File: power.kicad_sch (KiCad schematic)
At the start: 14 parts, among them J3 Conn_01x02, U1 TP4056-42-ESOP8, U11 TPS62170DSG

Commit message: finish power management
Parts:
- added D4: D, symbol Device:D
- added J4: USB_C_Receptacle_PowerOnly_6P, symbol Connector:USB_C_Receptacle_PowerOnly_6P
- added Q1: AO3401A, Package_TO_SOT_SMD:SOT-23, symbol Transistor_FET:AO3401A
- added R10: 100k, Resistor_SMD:R_0603_1608Metric, symbol Device:R
- added R6: 562k, Resistor_SMD:R_0603_1608Metric, symbol Device:R
- added R7: 180k, Resistor_SMD:R_0603_1608Metric, symbol Device:R
- added R8, R9: 5.1k, Resistor_SMD:R_0603_1608Metric, symbol Device:R
- C3, C4, C6, C7: footprint (none) -> Capacitor_SMD:C_0603_1608Metric
- D1: value LED -> GREEN; footprint (none) -> LED_SMD:LED_0603_1608Metric; LCSC (none) -> C965804; Manufacturer (none) -> XINGLIGHT; Manufacturer Part Number (none) -> XL-1608UGC-04
- D2: value LED -> RED; footprint (none) -> LED_SMD:LED_0603_1608Metric; LCSC (none) -> C965799; Manufacturer (none) -> XINGLIGHT; Manufacturer Part Number (none) -> XL-1608SURC-06
- J3: LCSC (none) -> C131337; Manufacturer (none) -> JST; Manufacturer Part Number (none) -> B2B-PH-K-S(LF)(SN)
- L1: value 22uH -> 2.2uH; LCSC C128694 -> C5349701; Manufacturer SXN -> APV; Manufacturer Part Number SMMS0630-220M -> APH0630T2R2M
- R2, R3, R4, R5: footprint (none) -> Resistor_SMD:R_0603_1608Metric
- U1: LCSC (none) -> C16581; Manufacturer (none) -> TOP POWER ASIC; Manufacturer Part Number (none) -> TP4056-42-ESOP8
- U11: LCSC (none) -> TI; Manufacturer (none) -> C124041; Manufacturer Part Number (none) -> TPS62170DSGR
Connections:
- net BAT+: now also C4.1, J3.1 (Pin_1), U1.5 (BAT), Q1.3 (D); no longer C6.1, U11.2 (VIN), U11.3 (EN)
- net GND: now also J4.A12 (GND), J4.B12 (GND), J4.S1 (SHIELD), R10.2, R7.1, R8.2, R9.2; no longer U11.5 (FB)
- net VBUS: now also D4.2 (A), J4.A9 (VBUS), J4.B9 (VBUS), Q1.1 (G), R10.1
- net +3.3V: now reaches C7.1, L1.2, R5.1, U11.6 (VOS)
- net +3.3V: now also R6.1
- new net: C6.1, D4.1 (K), Q1.2 (S), U11.2 (VIN), U11.3 (EN)
- new net: R6.2, R7.2, U11.5 (FB)
- new net: J4.A5 (CC1), R8.1
- new net: J4.B5 (CC2), R9.1
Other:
- note added: "Allow vbus to power the buck when no battery is plugged in"
- note added: "R_{1}"
- note added: "R_{2}"
- note added: "R_{2} = 180k V_{OUT} = 3.3V R_{1} = R_{2} x ((V_{OUT} / 0.8V) - 1) = 562k"
- note added: "Step-down converter"
- note removed: "NOT DONE SET OUTPUT V"
- moved on the sheet: C3, C4, C6, C7, D1, D2, J3, L1, R2, R3, R4, R5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

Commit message: led driver backlight, not finished
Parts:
- C3: value C -> 10uF
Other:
- moved on the sheet: Q1
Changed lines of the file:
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@@
 	)
 	(rectangle
-		(start 78.74 53.34)
-		(end 152.4 121.92)
+		(start 81.28 53.34)
+		(end 149.86 121.92)
 		(stroke
 			(width 0)
@@
 	)
 	(junction
-		(at 163.83 66.04)
-		(diameter 0)
-		(color 0 0 0 0)
-	)
-	(junction
 		(at 201.93 104.14)
 		(diameter 0)
@@
 	)
 	(junction
+		(at 165.1 66.04)
+		(diameter 0)
+		(color 0 0 0 0)
+	)
+	(junction
 		(at 68.58 66.04)
 		(diameter 0)
@@
 	(wire
 		(pts
-			(xy 163.83 66.04) (xy 171.45 66.04)
+			(xy 214.63 87.63) (xy 214.63 104.14)
 		)
 		(stroke
@@
 	(wire
 		(pts
-			(xy 214.63 87.63) (xy 214.63 104.14)
+			(xy 165.1 66.04) (xy 171.45 66.04)
 		)
 		(stroke
@@
 	(wire
 		(pts
-			(xy 163.83 66.04) (xy 163.83 74.93)
+			(xy 165.1 66.04) (xy 165.1 74.93)
 		)
 		(stroke
@@
 	(wire
 		(pts
+			(xy 160.02 82.55) (xy 158.75 82.55)
+		)
+		(stroke
+			(width 0)
+			(type default)
+		)
+	)
+	(wire
+		(pts
 			(xy 212.09 85.09) (xy 222.25 85.09)
 		)
@@
 	(wire
 		(pts
-			(xy 168.91 82.55) (xy 171.45 82.55)
+			(xy 170.18 82.55) (xy 171.45 82.55)
 		)
 		(stroke
@@
 	(wire
 		(pts
-			(xy 156.21 66.04) (xy 163.83 66.04)
+			(xy 156.21 66.04) (xy 165.1 66.04)
 		)
 		(stroke
@@
 			)
 		)
-		(property "Value" "C"
+		(property "Value" "10uF"
 			(at 133.35 71.1199 0)
 			(effects
@@
 	(symbol
 		(lib_id "Transistor_FET:AO3401A")
-		(at 163.83 80.01 90)
+		(at 165.1 80.01 90)
 		(mirror x)
 		(unit 1)
@@
 		(dnp no)
 		(property "Reference" "Q1"
-			(at 163.83 88.9 90)
+			(at 165.1 88.9 90)
 			(effects
 				(font
@@
 		)
 		(property "Value" "AO3401A"
-			(at 163.83 86.36 90)
+			(at 165.1 86.36 90)
 			(effects
 				(font
@@
 		)
 		(property "Footprint" "Package_TO_SOT_SMD:SOT-23"
-			(at 165.735 85.09 0)
+			(at 167.005 85.09 0)
 			(effects
 				(font
@@
 		)
 		(property "Datasheet" "http://www.aosmd.com/pdfs/datasheet/AO3401A.pdf"
-			(at 167.64 85.09 0)
+			(at 168.91 85.09 0)
 			(effects
 				(font
@@
 		)
 		(property "Description" "-4.0A Id, -30V Vds, P-Channel MOSFET, SOT-23"
-			(at 163.83 80.01 0)
+			(at 165.1 80.01 0)
 			(effects
 				(font
@@
 		)
 		(property "LCSC" "C347476"
-			(at 163.83 80.01 0)
+			(at 165.1 80.01 0)
 			(effects
 				(font
@@
 		)
 		(property "Manufacturer" "UMW"
-			(at 163.83 80.01 0)
+			(at 165.1 80.01 0)
 			(effects
 				(font
@@
 		)
 		(property "Manufacturer Part Number" "AO3401A"
-			(at 163.83 80.01 0)
+			(at 165.1 80.01 0)
 			(effects
 				(font

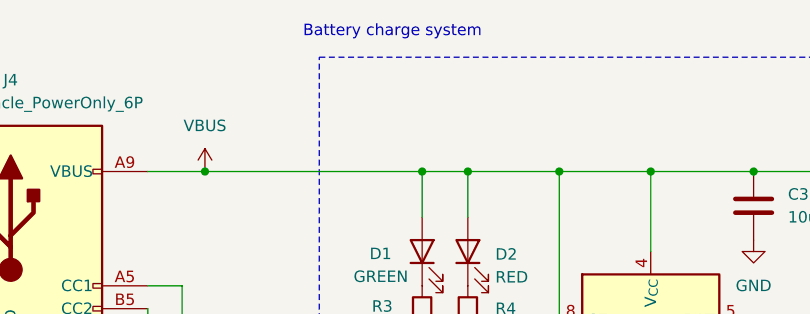
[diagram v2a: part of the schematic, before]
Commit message: add buttons and connect lcd
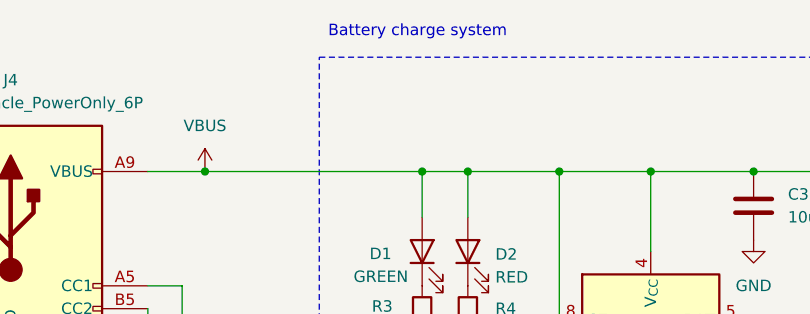
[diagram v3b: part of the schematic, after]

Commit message: remove backups, removed old chip
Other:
- note added: "I_{BAT}"
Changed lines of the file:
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@@
 		)
 	)
-	(text "0.5C = half the battery capacity per hour\n1000mAh => 500mA = I_{BAT} charge current\nR_{prog} = 1100 / I_{BAT} = 2.2k"
+	(text "I_{BAT}"
 		(exclude_from_sim no)
-		(at 123.952 113.03 0)
+		(at 131.572 100.076 0)
 		(effects
 			(font
@@
 		)
 	)
+	(text "0.5C = half the battery capacity per hour\n1000mAh => 500mA = I_{BAT} charge current\nR_{prog} = 1100 / I_{BAT} = 2.2k"
+		(exclude_from_sim no)
+		(at 97.282 112.776 0)
+		(effects
+			(font
+				(size 1.27 1.27)
+			)
+			(justify left)
+		)
+	)

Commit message: add rp2350 mcu
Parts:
- D4: footprint (none) -> Diode_SMD:D_SOD-323
- J4: footprint (none) -> Connector_USB:USB_C_Receptacle_GCT_USB4105-xx-A_16P_TopMnt_Horizontal
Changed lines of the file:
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@@
 			)
 		)
-		(property "Footprint" ""
+		(property "Footprint" "Connector_USB:USB_C_Receptacle_GCT_USB4105-xx-A_16P_TopMnt_Horizontal"
 			(at 50.8 71.12 0)
 			(effects
@@
 		)
 		(property "Description" "USB Power-Only 6P Type-C Receptacle connector"
+			(at 46.99 73.66 0)
+			(effects
+				(font
+					(size 1.27 1.27)
+				)
+				(hide yes)
+			)
+		)
+		(property "LCSC" ""
+			(at 46.99 73.66 0)
+			(effects
+				(font
+					(size 1.27 1.27)
+				)
+				(hide yes)
+			)
+		)
+		(property "Manufacturer" ""
+			(at 46.99 73.66 0)
+			(effects
+				(font
+					(size 1.27 1.27)
+				)
+				(hide yes)
+			)
+		)
+		(property "Manufacturer Part Number" ""
 			(at 46.99 73.66 0)
 			(effects
@@
 			)
 		)
-		(property "Footprint" ""
+		(property "Footprint" "Diode_SMD:D_SOD-323"
 			(at 171.45 78.74 0)
 			(effects

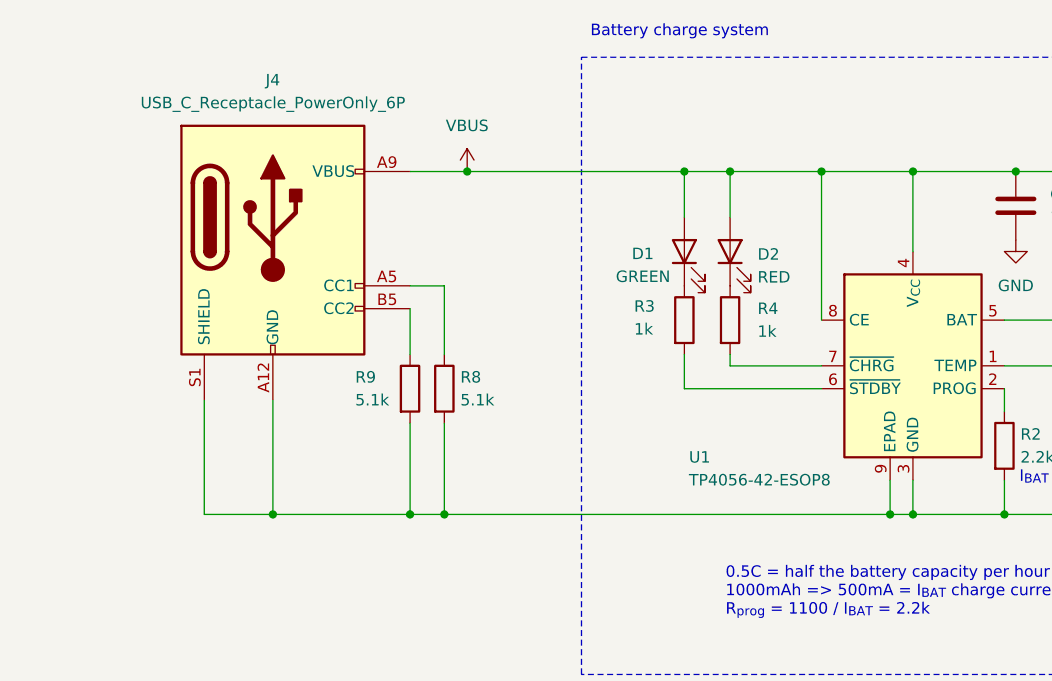
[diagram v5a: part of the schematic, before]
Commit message: add usb c connector
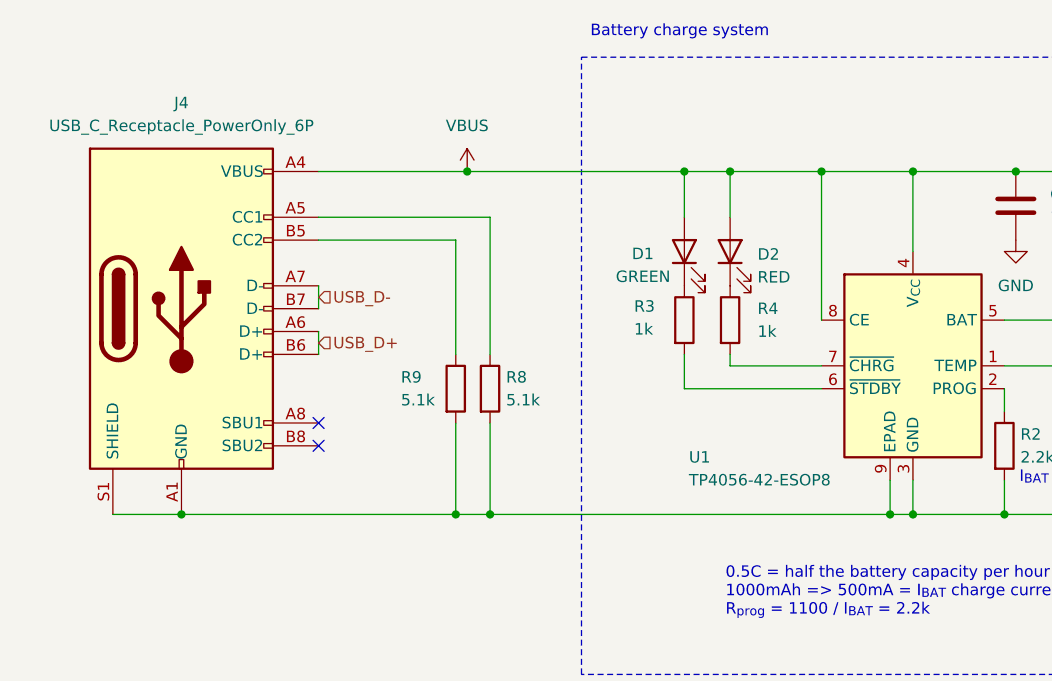
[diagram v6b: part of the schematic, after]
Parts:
- J4: symbol Connector:USB_C_Receptacle_PowerOnly_6P -> Connector:USB_C_Receptacle_USB2.0_16P; LCSC (none) -> C2765186; Manufacturer (none) -> SHOU HAN; Manufacturer Part Number (none) -> TYPE-C 16PIN 2MD(073)
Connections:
- net GND: now also J4.A1 (GND), J4.B1 (GND)
- net VBUS: now also J4.A4 (VBUS), J4.B4 (VBUS)
- new net USB_D+: J4.A6 (D+), J4.B6 (D+)
- new net USB_D-: J4.A7 (D-), J4.B7 (D-)
- no-connect marks 0 -> 2
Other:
- moved on the sheet: R8, R9

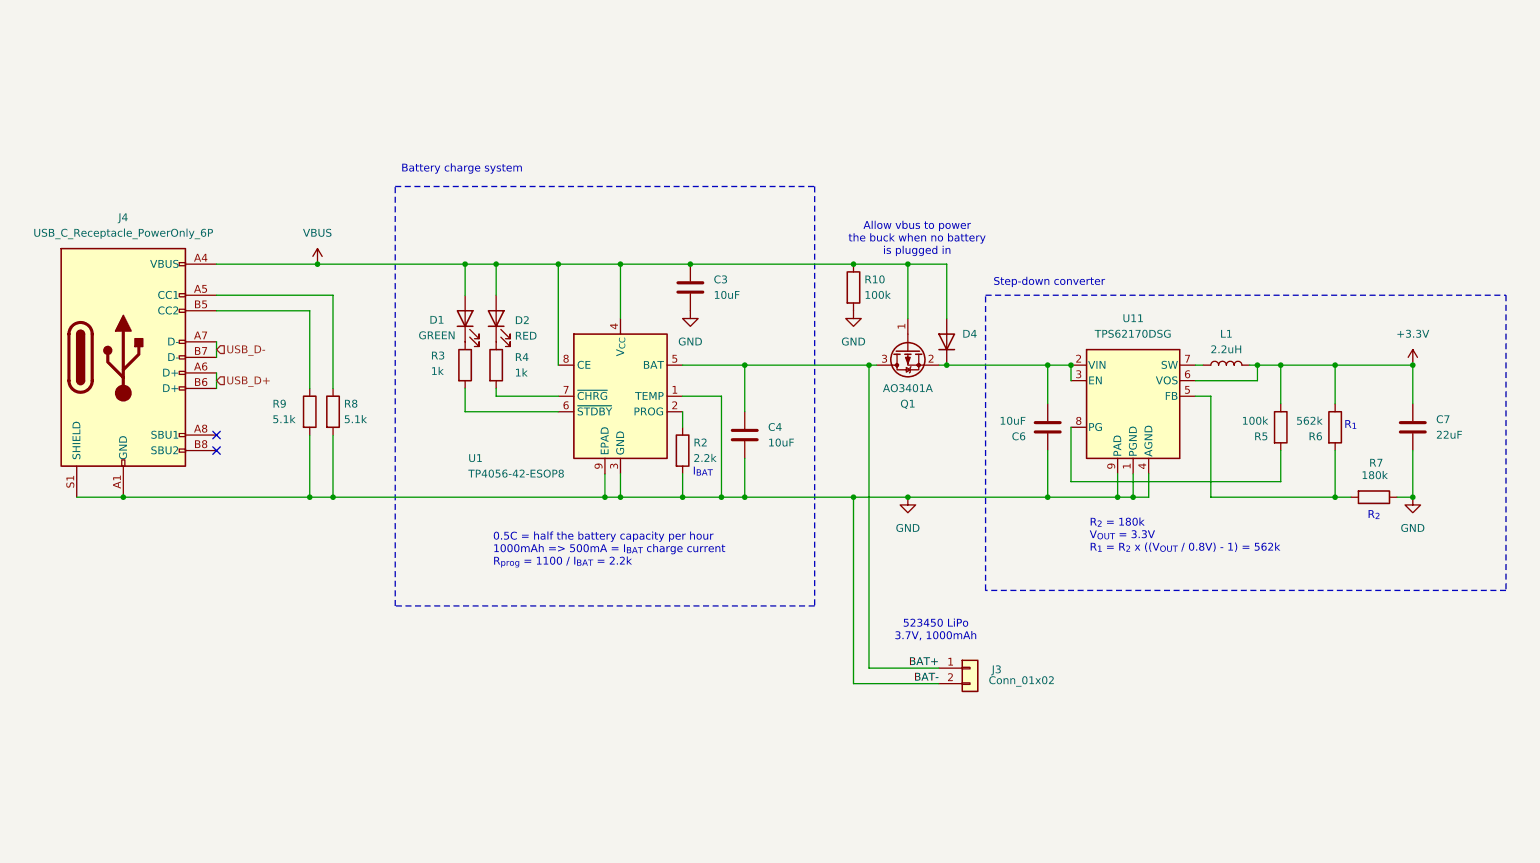
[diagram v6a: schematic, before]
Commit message: schematic functional and includes current test setup
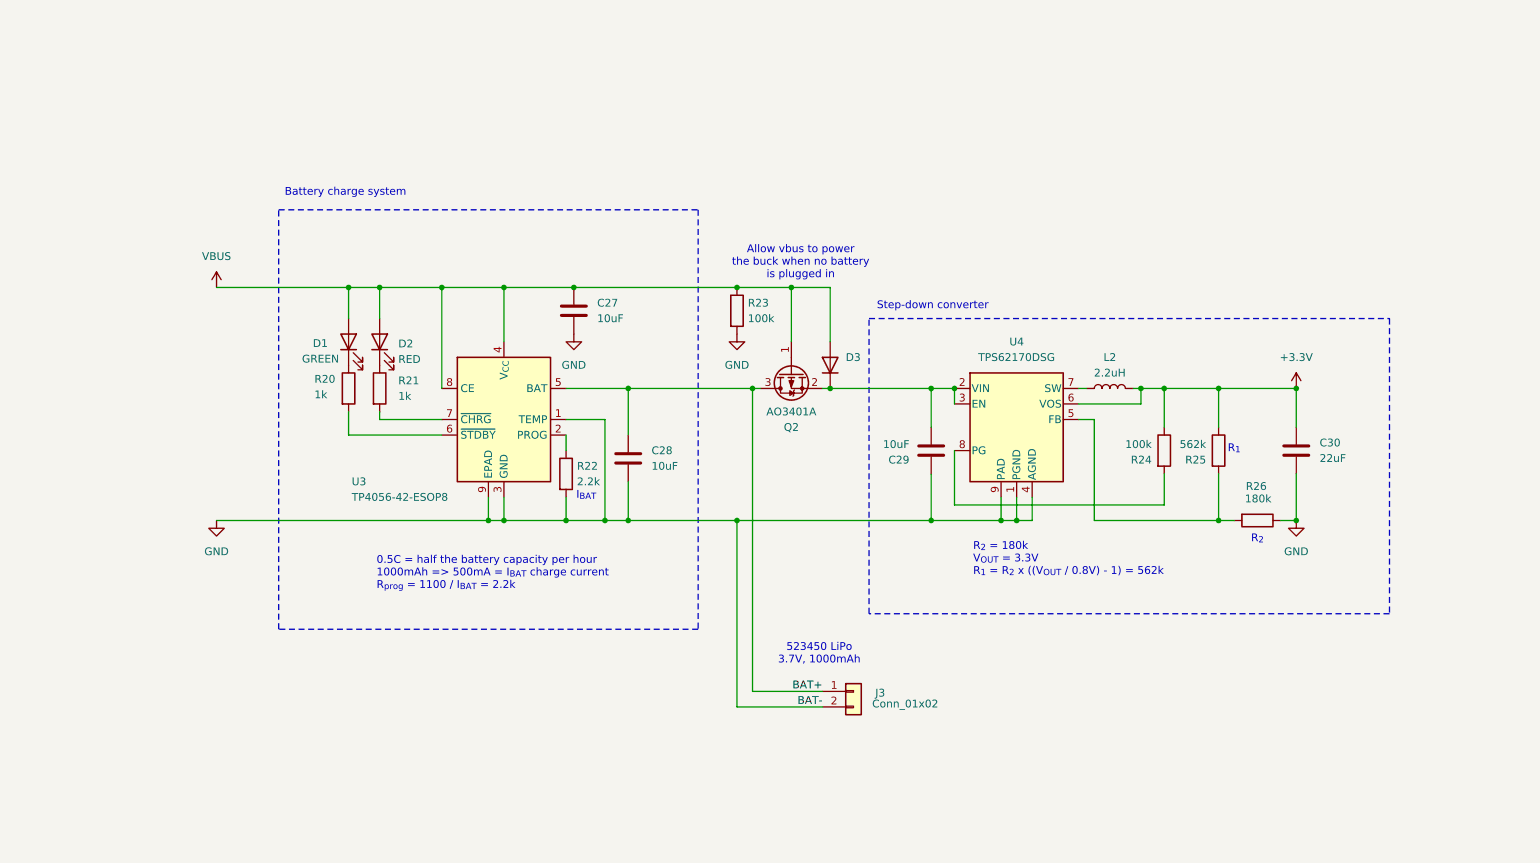
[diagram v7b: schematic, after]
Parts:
- removed J4: USB_C_Receptacle_PowerOnly_6P, Connector_USB:USB_C_Receptacle_GCT_USB4105-xx-A_16P_TopMnt_Horizontal, symbol Connector:USB_C_Receptacle_USB2.0_16P
- removed R8, R9: 5.1k, Resistor_SMD:R_0603_1608Metric, symbol Device:R
- renumbered C3 to C27, C4 to C28, C6 to C29, C7 to C30, D4 to D3, L1 to L2, Q1 to Q2, R3 to R20, R4 to R21, R2 to R22, R10 to R23, R5 to R24, R6 to R25, R7 to R26, U1 to U3, U11 to U4
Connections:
- no-connect marks 2 -> 0
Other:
- moved on the sheet: C27, C28, C29, C30, D1, D2, D3, J3, L2, Q2, R20, R21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

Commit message: fix usb and add esd diodes, some other checks
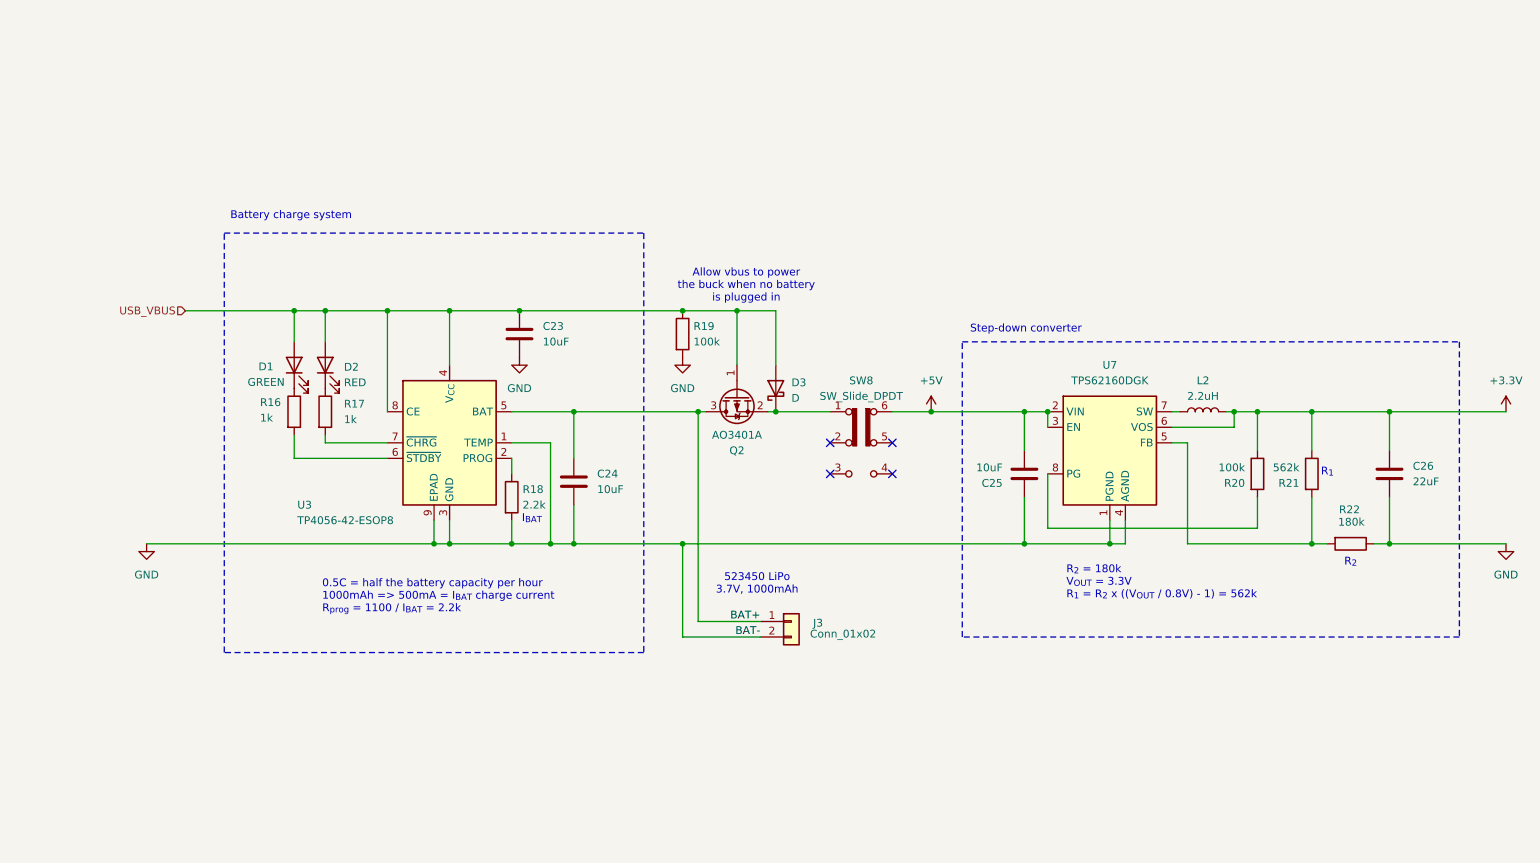
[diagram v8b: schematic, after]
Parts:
- removed C27, C28, C29: 10uF, Capacitor_SMD:C_0603_1608Metric, symbol Device:C
- removed C30: 22uF, Capacitor_SMD:C_0603_1608Metric, symbol Device:C
- removed D3: D, Diode_SMD:D_SOD-323, symbol Device:D
- removed R23, R24: 100k, Resistor_SMD:R_0603_1608Metric, symbol Device:R
- removed R25: 562k, Resistor_SMD:R_0603_1608Metric, symbol Device:R
- removed R26: 180k, Resistor_SMD:R_0603_1608Metric, symbol Device:R
- removed U4: TPS62170DSG, Package_SON:WSON-8-1EP_2x2mm_P0.5mm_EP0.9x1.6mm_ThermalVias, symbol Regulator_Switching:TPS62170DSG
- added C23, C24, C25: 10uF, Capacitor_SMD:C_0603_1608Metric, symbol Device:C
- added C26: 22uF, Capacitor_SMD:C_0603_1608Metric, symbol Device:C
- added D3: D, Diode_SMD:D_SMA, symbol Device:D_Schottky
- added R16, R17: 1k, Resistor_SMD:R_0603_1608Metric, symbol Device:R
- added R18: 2.2k, Resistor_SMD:R_0603_1608Metric, symbol Device:R
- added R19: 100k, Resistor_SMD:R_0603_1608Metric, symbol Device:R
- added SW8: SW_Slide_DPDT, Button_Switch_SMD:SW_DPDT_CK_JS202011JCQN, symbol Switch:SW_Slide_DPDT
- added U7: TPS62160DGK, Package_SO:MSOP-8_3x3mm_P0.65mm, symbol Regulator_Switching:TPS62160DGK
- R20: value 1k -> 100k
- R21: value 1k -> 562k
- R22: value 2.2k -> 180k
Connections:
- net +3.3V: now also R20.1, R21.1, C26.1, U7.6 (VOS)
- net BAT+: now also C24.1
- net GND: now also R22.1, C23.2, C24.2, C25.2, C26.2, R18.2, R19.2, U7.1 (PGND), U7.4 (AGND); no longer R22.2
- net at Q2.2 (S): now also D3.1 (K), SW8.1 (A)
- net at L2.1: now also U7.7 (SW)
- net at D1.1 (K): now also R16.1; no longer R20.1
- net at R20.2: now also U7.8 (PG); no longer U3.6 (~{STDBY})
- net at D2.1 (K): now also R17.1; no longer R21.1
- net at R21.2: now also R22.2, U7.5 (FB); no longer U3.7 (~{CHRG})
- net at U3.2 (PROG): now also R18.1; no longer R22.1
- net VBUS renamed USB_VBUS
- net USB_VBUS: now also C23.1, D3.2 (A), R19.1
- new net: R16.2, U3.6 (~{STDBY})
- new net: R17.2, U3.7 (~{CHRG})
- new net +5V: C25.1, SW8.6 (C), U7.2 (VIN), U7.3 (EN)
- no-connect marks 0 -> 4
